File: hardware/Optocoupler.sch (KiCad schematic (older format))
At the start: 6 parts, among them U2 VOH1016AB-T2

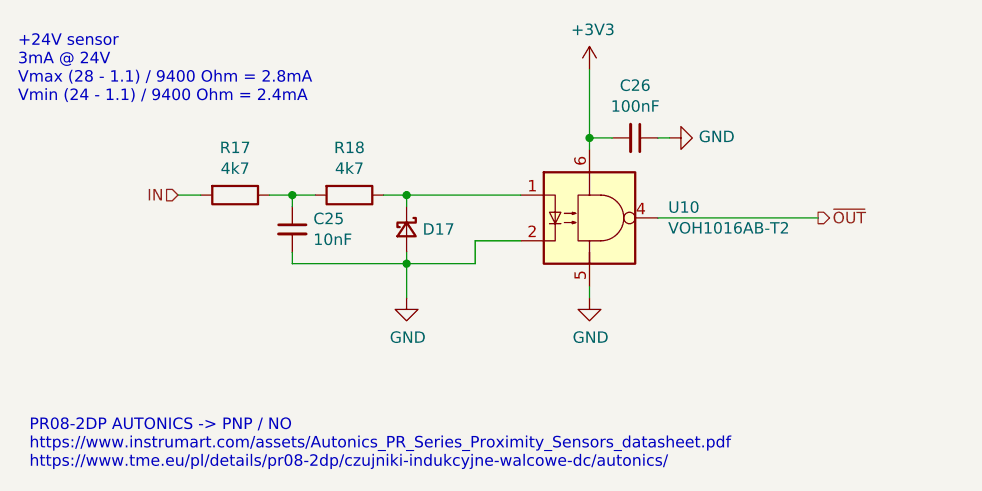
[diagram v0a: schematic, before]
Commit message: 1. added 2X20 connector, \n 2. changed the footprints of schootkies and zenner diodes to a bigger ones, \n 3. changed pcb layout entirely couse duck me, that connector i too duking BIG.
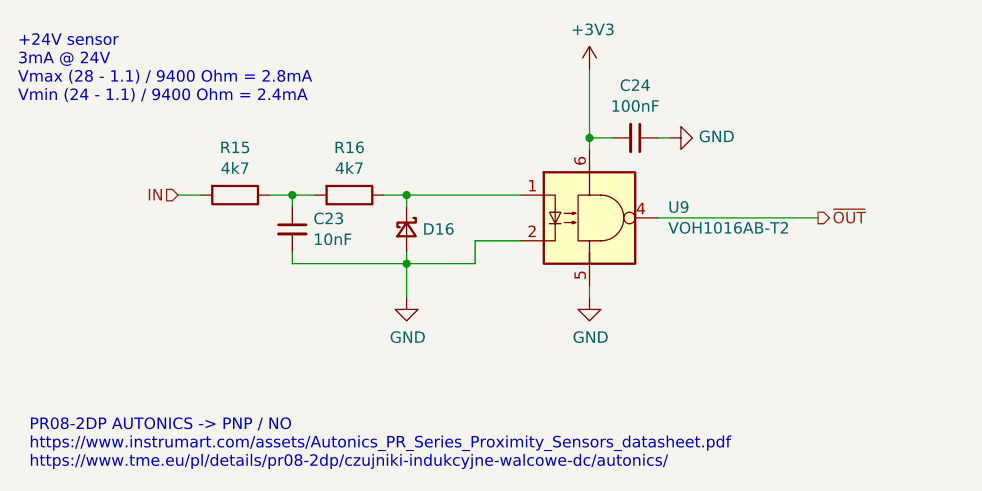
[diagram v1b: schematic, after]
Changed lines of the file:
@@
 $Descr A4 11693 8268
 encoding utf-8
-Sheet 7 20
+Sheet 6 20
 Title "Wheel Speed Sensor digital input"
 Date "2021-11-09"
@@
 AR Path="/61B82715/616CE551" Ref="#PWR049"  Part="1"
 AR Path="/61B8593E/616CE551" Ref="#PWR053"  Part="1"
-F 0 "#PWR053" H 6650 4250 50  0001 C CNN
+F 0 "#PWR049" H 6650 4250 50  0001 C CNN
 F 1 "GND" H 6655 4327 50  0000 C CNN
 F 2 "" H 6650 4500 50  0001 C CNN
@@
 AR Path="/61B82715/616CEB8B" Ref="#PWR048"  Part="1"
 AR Path="/61B8593E/616CEB8B" Ref="#PWR052"  Part="1"
-F 0 "#PWR052" H 6650 3350 50  0001 C CNN
+F 0 "#PWR048" H 6650 3350 50  0001 C CNN
 F 1 "+3V3" H 6665 3673 50  0000 C CNN
 F 2 "" H 6650 3500 50  0001 C CNN
@@
 AR Path="/61B82715/616D3668" Ref="C24"  Part="1"
 AR Path="/61B8593E/616D3668" Ref="C26"  Part="1"
-F 0 "C26" V 6621 3800 50  0000 C CNN
+F 0 "C24" V 6621 3800 50  0000 C CNN
 F 1 "100nF" V 6712 3800 50  0000 C CNN
 F 2 "Capacitor_SMD:C_0603_1608Metric" H 6850 3800 50  0001 C CNN
@@
 AR Path="/61B82715/616D3DA7" Ref="#PWR050"  Part="1"
 AR Path="/61B8593E/616D3DA7" Ref="#PWR054"  Part="1"
-F 0 "#PWR054" H 7000 3550 50  0001 C CNN
+F 0 "#PWR050" H 7000 3550 50  0001 C CNN
 F 1 "GND" V 7005 3672 50  0000 R CNN
 F 2 "" H 7000 3800 50  0001 C CNN
@@
 AR Path="/61B82715/618E4C31" Ref="D16"  Part="1"
 AR Path="/61B8593E/618E4C31" Ref="D17"  Part="1"
-F 0 "D17" V 5850 4270 50  0000 L CNN
+F 0 "D16" V 5850 4270 50  0000 L CNN
 F 1 "D_SCH" V 5895 4270 50  0001 L CNN
 F 2 "Diode_SMD:D_0603_1608Metric" V 5850 4200 50  0001 C CNN
@@
 AR Path="/61B82715/616CCBB0" Ref="C23"  Part="1"
 AR Path="/61B8593E/616CCBB0" Ref="C25"  Part="1"
-F 0 "C25" H 5442 4246 50  0000 L CNN
+F 0 "C23" H 5442 4246 50  0000 L CNN
 F 1 "10nF" H 5442 4155 50  0000 L CNN
 F 2 "Capacitor_SMD:C_0603_1608Metric" H 5350 4200 50  0001 C CNN
@@
 AR Path="/61B82715/616CC3EC" Ref="R16"  Part="1"
 AR Path="/61B8593E/616CC3EC" Ref="R18"  Part="1"
-F 0 "R18" V 5393 4050 50  0000 C CNN
+F 0 "R16" V 5393 4050 50  0000 C CNN
 F 1 "4k7" V 5484 4050 50  0000 C CNN
 F 2 "Resistor_SMD:R_0603_1608Metric" V 5530 4050 50  0001 C CNN
@@
 AR Path="/61B82715/619B83B9" Ref="#PWR047"  Part="1"
 AR Path="/61B8593E/619B83B9" Ref="#PWR051"  Part="1"
-F 0 "#PWR051" H 5850 4250 50  0001 C CNN
+F 0 "#PWR047" H 5850 4250 50  0001 C CNN
 F 1 "GND" H 5855 4327 50  0000 C CNN
 F 2 "" H 5850 4500 50  0001 C CNN
@@
 AR Path="/61B82715/616C86DF" Ref="U9"  Part="1"
 AR Path="/61B8593E/616C86DF" Ref="U10"  Part="1"
-F 0 "U10" H 6994 4196 50  0000 L CNN
+F 0 "U9" H 6994 4196 50  0000 L CNN
 F 1 "VOH1016AB-T2" H 6994 4105 50  0000 L CNN
 F 2 "Package_DIP:SMDIP-6_W7.62mm" H 6560 4150 50  0001 C CNN
@@
 AR Path="/61B82715/61932E16" Ref="R15"  Part="1"
 AR Path="/61B8593E/61932E16" Ref="R17"  Part="1"
-F 0 "R17" V 4893 4050 50  0000 C CNN
+F 0 "R15" V 4893 4050 50  0000 C CNN
 F 1 "4k7" V 4984 4050 50  0000 C CNN
 F 2 "Resistor_SMD:R_0603_1608Metric" V 5030 4050 50  0001 C CNN

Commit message: Updated to be compatible with KiCad 6.0.0, changed chematics layouts to fit in A4 worksheet and finished routing the rest of the signals.
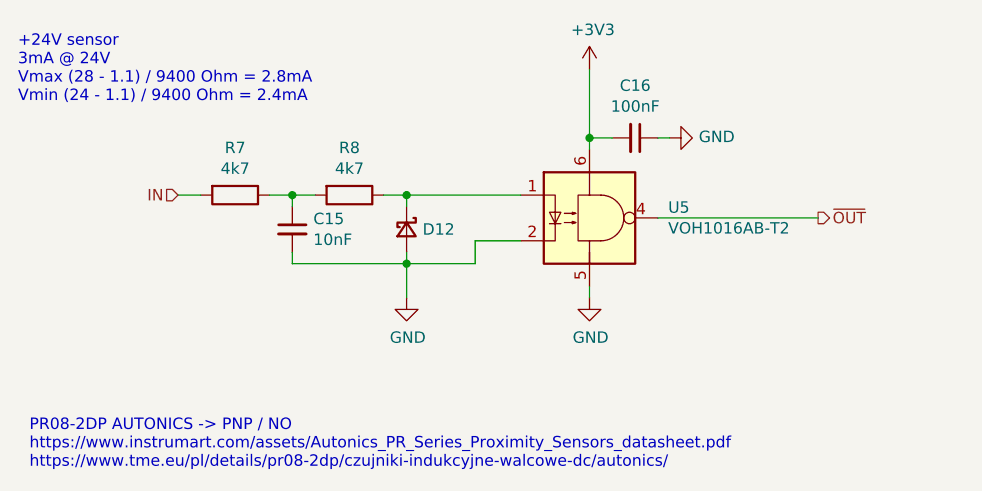
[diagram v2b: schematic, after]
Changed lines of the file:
@@
 $Descr A4 11693 8268
 encoding utf-8
-Sheet 6 20
+Sheet 17 24
 Title "Wheel Speed Sensor digital input"
 Date "2021-11-09"
@@
 AR Path="/61B82715/616CE551" Ref="#PWR049"  Part="1"
 AR Path="/61B8593E/616CE551" Ref="#PWR053"  Part="1"
-F 0 "#PWR049" H 6650 4250 50  0001 C CNN
+AR Path="/62DA6EC2/62EDE8B2/616CE551" Ref="#PWR?"  Part="1"
+AR Path="/62DA6EC2/62EDE8B6/616CE551" Ref="#PWR?"  Part="1"
+AR Path="/62DA6EC2/62EDE8BA/616CE551" Ref="#PWR?"  Part="1"
+AR Path="/62DA6EC2/62EDE8BE/616CE551" Ref="#PWR?"  Part="1"
+AR Path="/62DA6EC2/62EDE8D6/616CE551" Ref="#PWR?"  Part="1"
+F 0 "#PWR033" H 6650 4250 50  0001 C CNN
 F 1 "GND" H 6655 4327 50  0000 C CNN
 F 2 "" H 6650 4500 50  0001 C CNN
@@
 AR Path="/61B82715/616CEB8B" Ref="#PWR048"  Part="1"
 AR Path="/61B8593E/616CEB8B" Ref="#PWR052"  Part="1"
-F 0 "#PWR048" H 6650 3350 50  0001 C CNN
+AR Path="/62DA6EC2/62EDE8B2/616CEB8B" Ref="#PWR?"  Part="1"
+AR Path="/62DA6EC2/62EDE8B6/616CEB8B" Ref="#PWR?"  Part="1"
+AR Path="/62DA6EC2/62EDE8BA/616CEB8B" Ref="#PWR?"  Part="1"
+AR Path="/62DA6EC2/62EDE8BE/616CEB8B" Ref="#PWR?"  Part="1"
+AR Path="/62DA6EC2/62EDE8D6/616CEB8B" Ref="#PWR?"  Part="1"
+F 0 "#PWR032" H 6650 3350 50  0001 C CNN
 F 1 "+3V3" H 6665 3673 50  0000 C CNN
 F 2 "" H 6650 3500 50  0001 C CNN
@@
 AR Path="/61B82715/616D3668" Ref="C24"  Part="1"
 AR Path="/61B8593E/616D3668" Ref="C26"  Part="1"
-F 0 "C24" V 6621 3800 50  0000 C CNN
+AR Path="/62DA6EC2/62EDE8B2/616D3668" Ref="C?"  Part="1"
+AR Path="/62DA6EC2/62EDE8B6/616D3668" Ref="C?"  Part="1"
+AR Path="/62DA6EC2/62EDE8BA/616D3668" Ref="C?"  Part="1"
+AR Path="/62DA6EC2/62EDE8BE/616D3668" Ref="C?"  Part="1"
+AR Path="/62DA6EC2/62EDE8D6/616D3668" Ref="C?"  Part="1"
+F 0 "C16" V 6621 3800 50  0000 C CNN
 F 1 "100nF" V 6712 3800 50  0000 C CNN
 F 2 "Capacitor_SMD:C_0603_1608Metric" H 6850 3800 50  0001 C CNN
@@
 AR Path="/61B82715/616D3DA7" Ref="#PWR050"  Part="1"
 AR Path="/61B8593E/616D3DA7" Ref="#PWR054"  Part="1"
-F 0 "#PWR050" H 7000 3550 50  0001 C CNN
+AR Path="/62DA6EC2/62EDE8B2/616D3DA7" Ref="#PWR?"  Part="1"
+AR Path="/62DA6EC2/62EDE8B6/616D3DA7" Ref="#PWR?"  Part="1"
+AR Path="/62DA6EC2/62EDE8BA/616D3DA7" Ref="#PWR?"  Part="1"
+AR Path="/62DA6EC2/62EDE8BE/616D3DA7" Ref="#PWR?"  Part="1"
+AR Path="/62DA6EC2/62EDE8D6/616D3DA7" Ref="#PWR?"  Part="1"
+F 0 "#PWR034" H 7000 3550 50  0001 C CNN
 F 1 "GND" V 7005 3672 50  0000 R CNN
 F 2 "" H 7000 3800 50  0001 C CNN
@@
 AR Path="/61B82715/618E4C31" Ref="D16"  Part="1"
 AR Path="/61B8593E/618E4C31" Ref="D17"  Part="1"
-F 0 "D16" V 5850 4270 50  0000 L CNN
+AR Path="/62DA6EC2/62EDE8B2/618E4C31" Ref="D?"  Part="1"
+AR Path="/62DA6EC2/62EDE8B6/618E4C31" Ref="D?"  Part="1"
+AR Path="/62DA6EC2/62EDE8BA/618E4C31" Ref="D?"  Part="1"
+AR Path="/62DA6EC2/62EDE8BE/618E4C31" Ref="D?"  Part="1"
+AR Path="/62DA6EC2/62EDE8D6/618E4C31" Ref="D?"  Part="1"
+F 0 "D12" V 5850 4270 50  0000 L CNN
 F 1 "D_SCH" V 5895 4270 50  0001 L CNN
 F 2 "Diode_SMD:D_0603_1608Metric" V 5850 4200 50  0001 C CNN
@@
 AR Path="/61B82715/616CCBB0" Ref="C23"  Part="1"
 AR Path="/61B8593E/616CCBB0" Ref="C25"  Part="1"
-F 0 "C23" H 5442 4246 50  0000 L CNN
+AR Path="/62DA6EC2/62EDE8B2/616CCBB0" Ref="C?"  Part="1"
+AR Path="/62DA6EC2/62EDE8B6/616CCBB0" Ref="C?"  Part="1"
+AR Path="/62DA6EC2/62EDE8BA/616CCBB0" Ref="C?"  Part="1"
+AR Path="/62DA6EC2/62EDE8BE/616CCBB0" Ref="C?"  Part="1"
+AR Path="/62DA6EC2/62EDE8D6/616CCBB0" Ref="C?"  Part="1"
+F 0 "C15" H 5442 4246 50  0000 L CNN
 F 1 "10nF" H 5442 4155 50  0000 L CNN
 F 2 "Capacitor_SMD:C_0603_1608Metric" H 5350 4200 50  0001 C CNN
@@
 AR Path="/61B82715/616CC3EC" Ref="R16"  Part="1"
 AR Path="/61B8593E/616CC3EC" Ref="R18"  Part="1"
-F 0 "R16" V 5393 4050 50  0000 C CNN
+AR Path="/62DA6EC2/62EDE8B2/616CC3EC" Ref="R?"  Part="1"
+AR Path="/62DA6EC2/62EDE8B6/616CC3EC" Ref="R?"  Part="1"
+AR Path="/62DA6EC2/62EDE8BA/616CC3EC" Ref="R?"  Part="1"
+AR Path="/62DA6EC2/62EDE8BE/616CC3EC" Ref="R?"  Part="1"
+AR Path="/62DA6EC2/62EDE8D6/616CC3EC" Ref="R?"  Part="1"
+F 0 "R8" V 5393 4050 50  0000 C CNN
 F 1 "4k7" V 5484 4050 50  0000 C CNN
 F 2 "Resistor_SMD:R_0603_1608Metric" V 5530 4050 50  0001 C CNN
@@
 AR Path="/61B82715/619B83B9" Ref="#PWR047"  Part="1"
 AR Path="/61B8593E/619B83B9" Ref="#PWR051"  Part="1"
-F 0 "#PWR047" H 5850 4250 50  0001 C CNN
+AR Path="/62DA6EC2/62EDE8B2/619B83B9" Ref="#PWR?"  Part="1"
+AR Path="/62DA6EC2/62EDE8B6/619B83B9" Ref="#PWR?"  Part="1"
+AR Path="/62DA6EC2/62EDE8BA/619B83B9" Ref="#PWR?"  Part="1"
+AR Path="/62DA6EC2/62EDE8BE/619B83B9" Ref="#PWR?"  Part="1"
+AR Path="/62DA6EC2/62EDE8D6/619B83B9" Ref="#PWR?"  Part="1"
+F 0 "#PWR031" H 5850 4250 50  0001 C CNN
 F 1 "GND" H 5855 4327 50  0000 C CNN
 F 2 "" H 5850 4500 50  0001 C CNN
@@
 AR Path="/61B82715/616C86DF" Ref="U9"  Part="1"
 AR Path="/61B8593E/616C86DF" Ref="U10"  Part="1"
-F 0 "U9" H 6994 4196 50  0000 L CNN
+AR Path="/62DA6EC2/62EDE8B2/616C86DF" Ref="U?"  Part="1"
+AR Path="/62DA6EC2/62EDE8B6/616C86DF" Ref="U?"  Part="1"
+AR Path="/62DA6EC2/62EDE8BA/616C86DF" Ref="U?"  Part="1"
+AR Path="/62DA6EC2/62EDE8BE/616C86DF" Ref="U?"  Part="1"
+AR Path="/62DA6EC2/62EDE8D6/616C86DF" Ref="U?"  Part="1"
+F 0 "U5" H 6994 4196 50  0000 L CNN
 F 1 "VOH1016AB-T2" H 6994 4105 50  0000 L CNN
 F 2 "Package_DIP:SMDIP-6_W7.62mm" H 6560 4150 50  0001 C CNN
@@
 AR Path="/61B82715/61932E16" Ref="R15"  Part="1"
 AR Path="/61B8593E/61932E16" Ref="R17"  Part="1"
-F 0 "R15" V 4893 4050 50  0000 C CNN
+AR Path="/62DA6EC2/62EDE8B2/61932E16" Ref="R?"  Part="1"
+AR Path="/62DA6EC2/62EDE8B6/61932E16" Ref="R?"  Part="1"
+AR Path="/62DA6EC2/62EDE8BA/61932E16" Ref="R?"  Part="1"
+AR Path="/62DA6EC2/62EDE8BE/61932E16" Ref="R?"  Part="1"
+AR Path="/62DA6EC2/62EDE8D6/61932E16" Ref="R?"  Part="1"
+F 0 "R7" V 4893 4050 50  0000 C CNN
 F 1 "4k7" V 4984 4050 50  0000 C CNN
 F 2 "Resistor_SMD:R_0603_1608Metric" V 5030 4050 50  0001 C CNN
